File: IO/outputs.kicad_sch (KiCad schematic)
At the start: 12 parts, among them J10 AudioJack2_SwitchT, Q1 BC847C, Q3 BC857C

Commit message: Minor fixes
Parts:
- D7: value LED_Dual_AAKK -> LTST-C195TGKRKT
- H3: value MountingHole -> VLP lightpipe
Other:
- company: (none) -> GuavTek
- title: (none) -> M2IDI - CV16 IO
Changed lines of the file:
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@@
 (kicad_sch (version 20230121) (generator eeschema)
   (paper "A4")
+  (title_block
+    (title "M2IDI - CV16 IO")
+    (date "2023-05-10")
+    (rev "3.0")
+    (company "GuavTek")
+  )
   (junction (at 130.81 93.98) (diameter 0) (color 0 0 0 0)
   )
@@
       (effects (font (size 1.27 1.27)) (justify left))
     )
-    (property "Value" "LED_Dual_AAKK" (at 153.924 117.3553 90)
+    (property "Value" "LTST-C195TGKRKT" (at 153.924 117.3553 90)
       (effects (font (size 1.27 1.27)) (justify left))
     )
@@
       (effects (font (size 1.27 1.27)) (justify left))
     )
-    (property "Value" "MountingHole" (at 179.705 118.7523 0)
-      (effects (font (size 1.27 1.27)) (justify left))
-    )
+    (property "Value" "VLP lightpipe" (at 179.705 118.7523 0)
+      (effects (font (size 1.27 1.27)) (justify left))
+    )

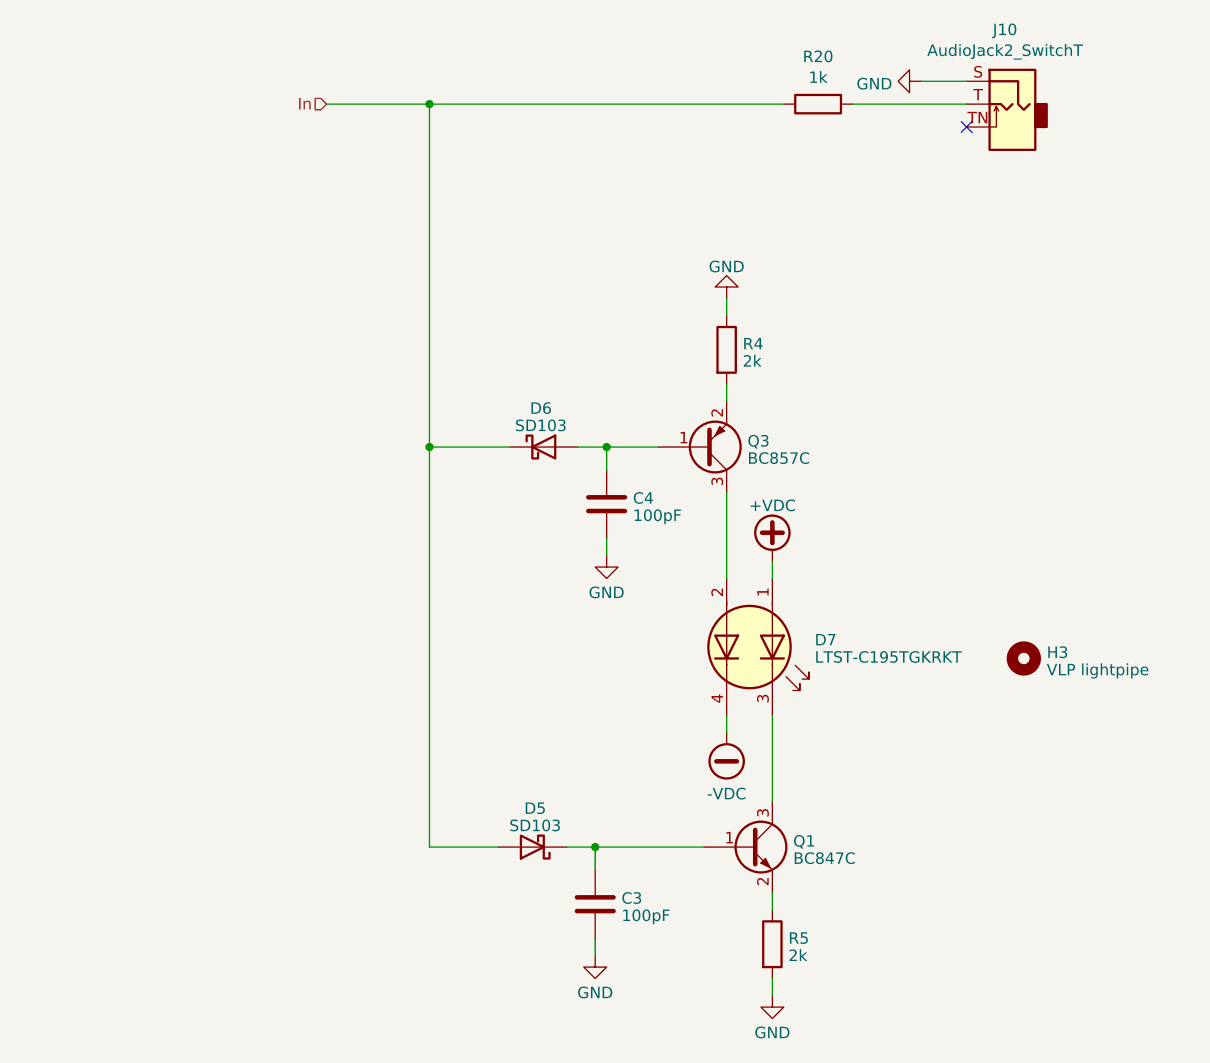
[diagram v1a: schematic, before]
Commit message: Add message about peak-detectors on IO leds
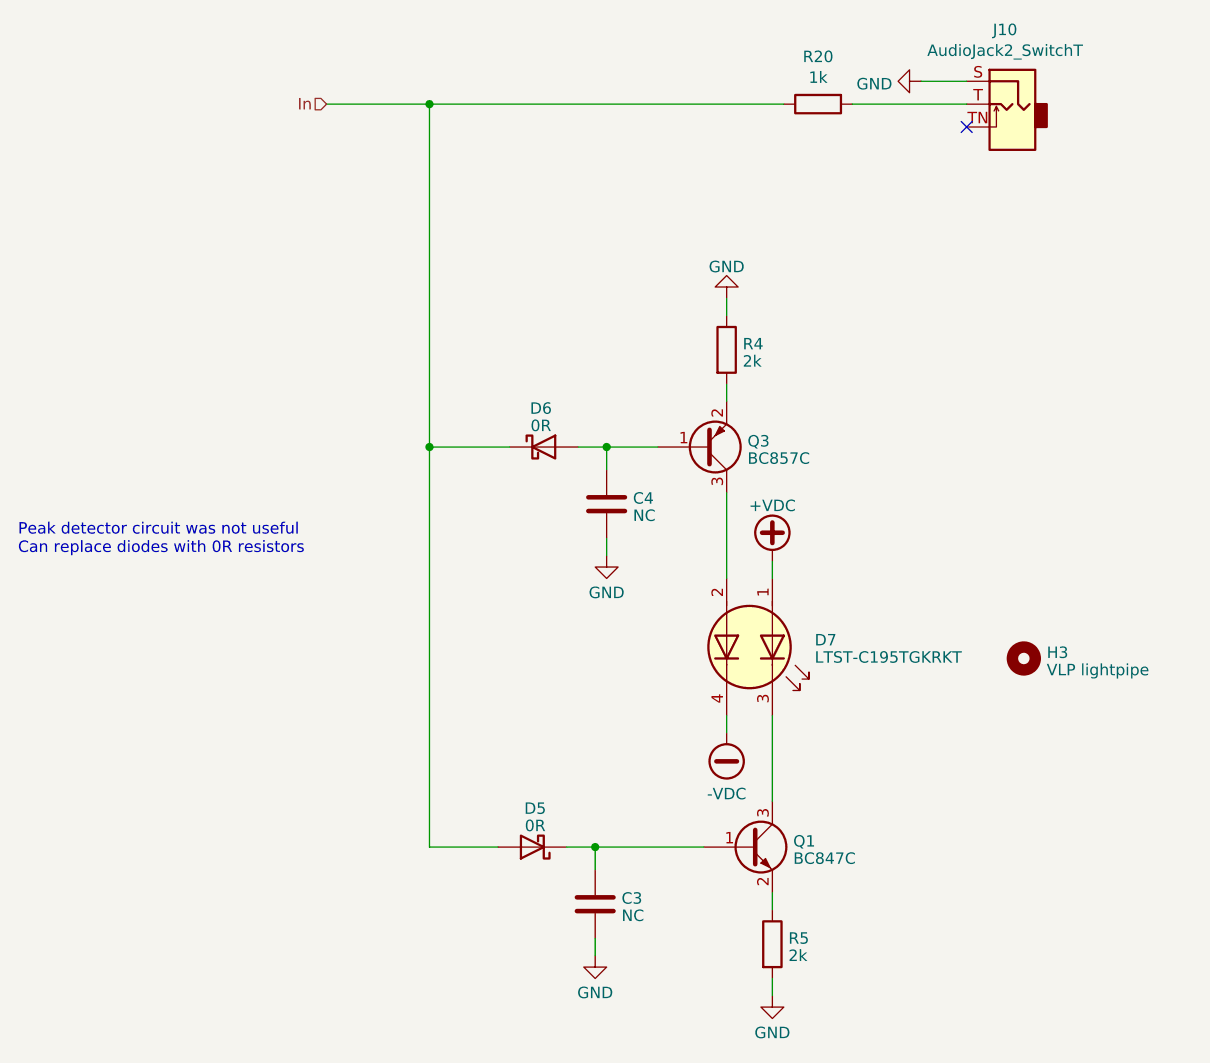
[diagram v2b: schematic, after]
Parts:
- C3, C4: value 100pF -> NC
- D5, D6: value SD103 -> 0R
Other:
- note added: "Peak detector circuit was not useful Can replace diodes with 0R resistors"
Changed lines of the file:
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@@
     (stroke (width 0) (type default))
+  )
+  (text "Peak detector circuit was not useful\nCan replace diodes with 0R resistors"
+    (at 65.405 106.045 0)
+    (effects (font (size 1.27 1.27)) (justify left bottom))
   )
   (hierarchical_label "In" (shape input) (at 99.695 55.88 180) (fields_autoplaced)
@@
       (effects (font (size 1.27 1.27)))
     )
-    (property "Value" "SD103" (at 122.8725 136.0711 0)
+    (property "Value" "0R" (at 122.8725 136.0711 0)
       (effects (font (size 1.27 1.27)))
     )
@@
       (effects (font (size 1.27 1.27)) (justify left))
     )
-    (property "Value" "100pF" (at 132.461 146.0573 0)
+    (property "Value" "NC" (at 132.461 146.0573 0)
       (effects (font (size 1.27 1.27)) (justify left))
     )
@@
       (effects (font (size 1.27 1.27)) (justify left))
     )
-    (property "Value" "100pF" (at 133.731 101.6073 0)
+    (property "Value" "NC" (at 133.731 101.6073 0)
       (effects (font (size 1.27 1.27)) (justify left))
     )
@@
       (effects (font (size 1.27 1.27)))
     )
-    (property "Value" "SD103" (at 123.5075 91.6211 0)
-      (effects (font (size 1.27 1.27)))
-    )
+    (property "Value" "0R" (at 123.5075 91.6211 0)
+      (effects (font (size 1.27 1.27)))
+    )

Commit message: Remove IO peak-detectors
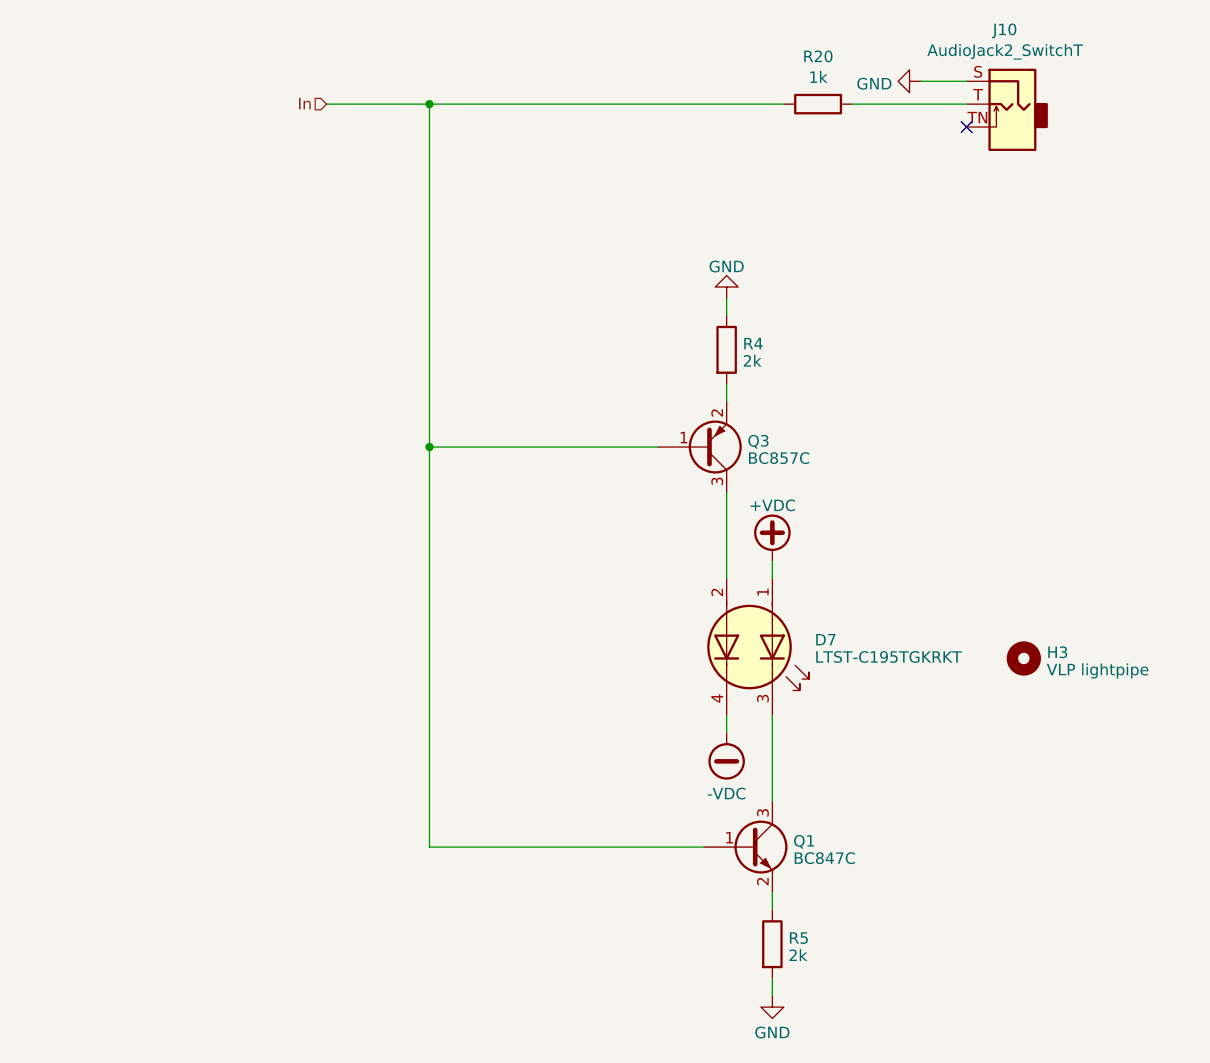
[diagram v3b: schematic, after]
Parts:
- removed C3, C4: NC, Capacitor_SMD:C_0603_1608Metric, symbol Device:C
- removed D5, D6: 0R, Diode_SMD:D_SOD-323_HandSoldering, symbol Device:D_Schottky
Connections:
- net In: now also Q1.1 (B), Q3.1 (B)
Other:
- note removed: "Peak detector circuit was not useful Can replace diodes with 0R resistors"

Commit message: Update to kicad 8
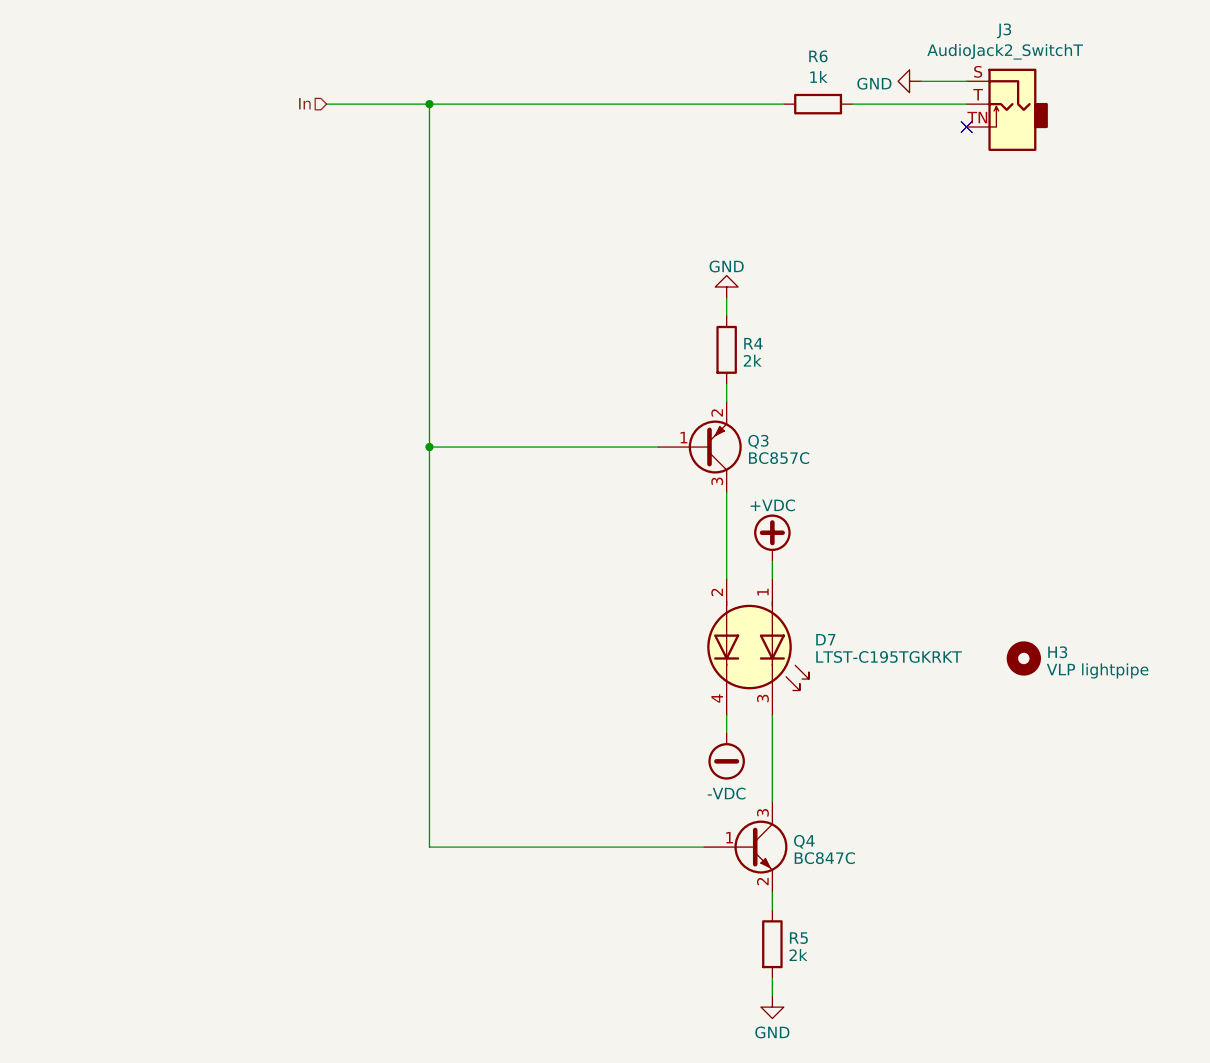
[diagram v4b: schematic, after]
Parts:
- renumbered J10 to J3, Q1 to Q4, R20 to R6
